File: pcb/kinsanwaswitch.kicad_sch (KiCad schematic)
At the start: 8 parts, among them J1 Conn_01x05, J2 Conn_01x02, U1 74LVC1G14

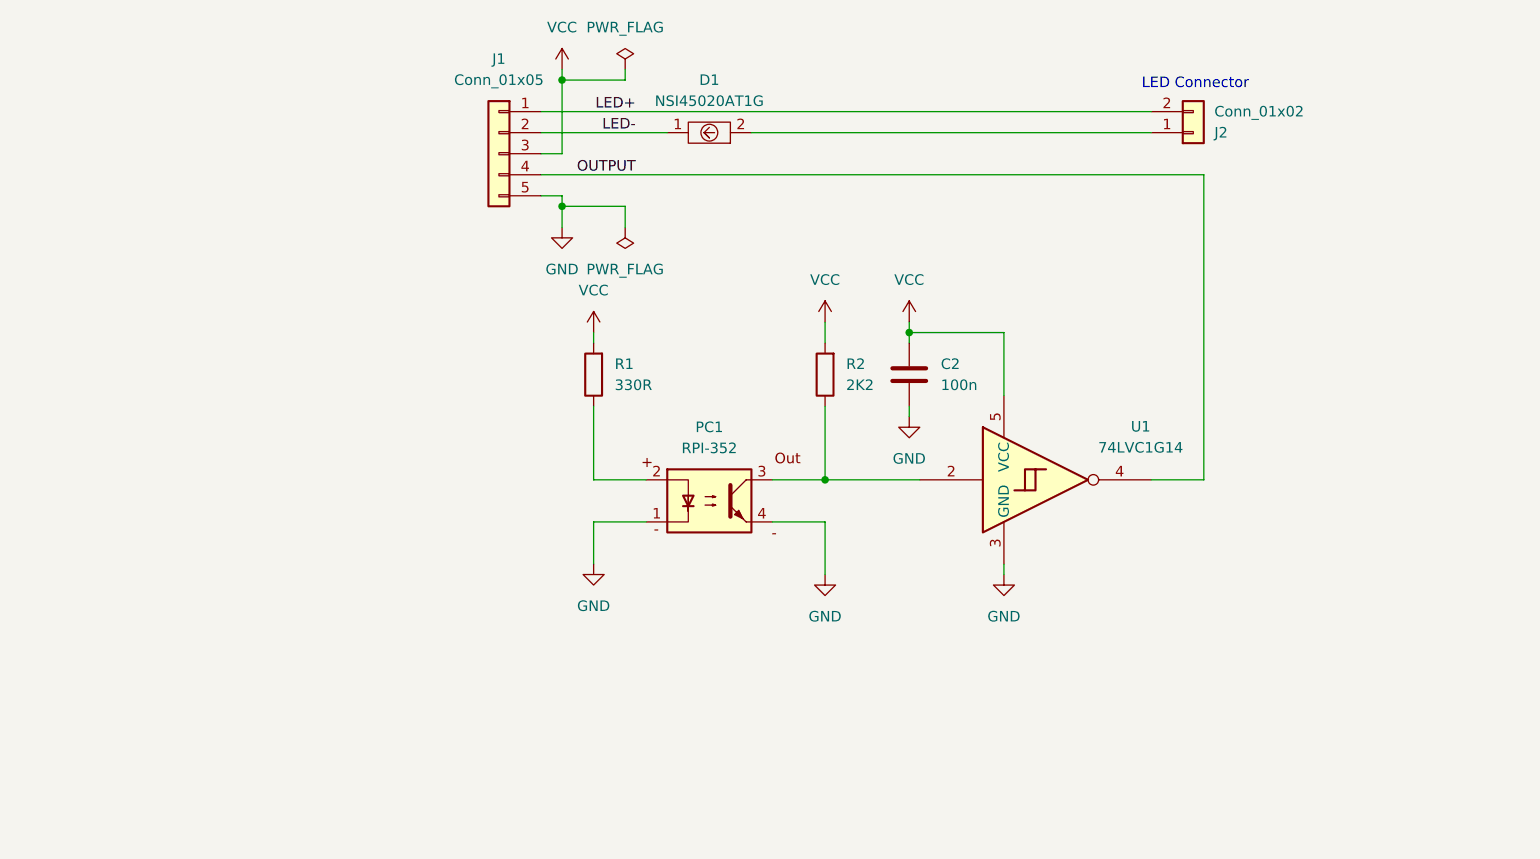
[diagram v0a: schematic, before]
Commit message: add name and dates to sheets
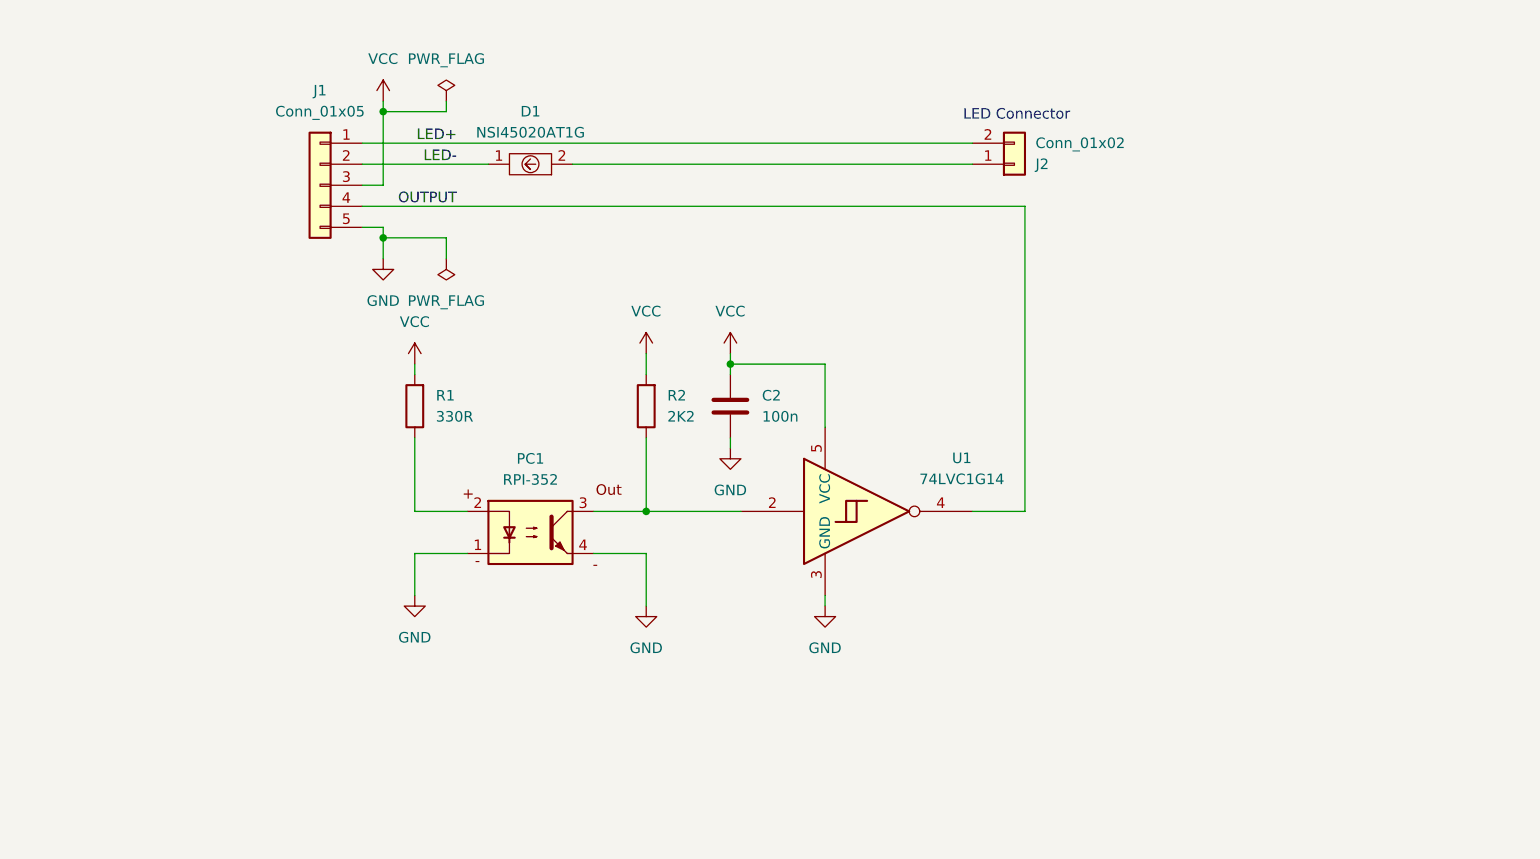
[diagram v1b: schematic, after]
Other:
- company: (none) -> Alexander Knapik
- title: (none) -> KINSANWASWITCH
- moved on the sheet: C2, D1, J1, J2, PC1, R1, R2, U1

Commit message: revision 1.0 PCB
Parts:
- removed D1: NSI45020AT1G, Diode_SMD:D_SOD-123, symbol RPI-221:NSI45020AT1G
- removed J1: Conn_01x05, Connector_JST:JST_PH_S5B-PH-K_1x05_P2.00mm_Horizontal, symbol Connector_Generic:Conn_01x05
- removed J2: Conn_01x02, Connector_JST:JST_PH_S2B-PH-K_1x02_P2.00mm_Horizontal, symbol Connector_Generic:Conn_01x02
- added C1: 1u0, Capacitor_SMD:C_0603_1608Metric, symbol Device:C
- added C3: 100n, Capacitor_SMD:C_0603_1608Metric, symbol Device:C
- added D2: 1N5819HW-7-F, Diode_SMD:D_SOD-123, symbol Device:D_Schottky
- added FID1, FID2: Fiducial, Fiducial:Fiducial_0.5mm_Mask1mm, symbol Mechanical:Fiducial
- added J1: SM05B-PASS-TBT, Connector_JST_PA:JST_PH_S5B-PH-SM4-TB_1x05-1MP_P2.00mm_Horizontal, symbol Connector_Generic_MountingPin:Conn_01x05_MountingPin
- added R3: 10R, Resistor_SMD:R_0603_1608Metric, symbol Device:R
- added SYM1: Logo_Open_Hardware_Small, Symbol:OSHW-Logo_5.7x6mm_SilkScreen, symbol Graphic:Logo_Open_Hardware_Small
- C2: footprint Resistor_SMD:R_0603_1608Metric_Pad0.98x0.95mm_HandSolder -> Capacitor_SMD:C_0603_1608Metric
- PC1: value RPI-352 -> RPI-0352E
- R1: footprint Resistor_SMD:R_0603_1608Metric_Pad0.98x0.95mm_HandSolder -> Resistor_SMD:R_0603_1608Metric
- R2: value 2K2 -> 47k; footprint Resistor_SMD:R_0603_1608Metric_Pad0.98x0.95mm_HandSolder -> Resistor_SMD:R_0603_1608Metric
- U1: value 74LVC1G14 -> 74HCT1G14; footprint Package_TO_SOT_SMD:SOT-353_SC-70-5_Handsoldering -> Package_TO_SOT_SMD:SC-74A-5_1.55x2.9mm_P0.95mm
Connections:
- net GND: now also C1.2, C3.2, J1.5 (Pin_5), J1.MP (MountPin)
- net LED+: now also J1.1 (Pin_1)
- net LED-: now also J1.2 (Pin_2)
- net VCC: now also D2.1 (K)
- net OUTPUT: no longer names the net of U1.4
- net OUTPUT: now also R3.1
- new net +5V: C1.1, D2.2 (A), J1.3 (Pin_3)
- new net N.O.: C3.1, J1.4 (Pin_4), R3.2
- no-connect marks 0 -> 2
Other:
- note added: "4.7 V"
- note added: "~300 mV drop @ 100 mA"
- note removed: "LED Connector"
- moved on the sheet: C2, PC1, R1, R2, U1
